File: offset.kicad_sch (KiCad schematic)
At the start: 52 parts

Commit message: More work in progres
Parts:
- removed C? (x3): 100n, symbol Device:C
- removed C? (x2): 1u, symbol Device:C
- removed R? (x3): 100k, symbol Device:R
- removed R? (x6): 158, symbol Device:R
- removed R? (x3): 309, symbol Device:R
- removed R?: 10k2, symbol Device:R
- removed R? (x2): 620, symbol Device:R
- removed R?: 80k6, symbol Device:R
- removed R?: 40k1, symbol Device:R
- removed R? (x2): 2k49, symbol Device:R
- removed R? (x2): 100, symbol Device:R
- removed R?: 20k, symbol Device:R
- removed R?: 1k24, symbol Device:R
- removed U? (x3): OPA2189D, Package_SO:SOIC-8_3.9x4.9mm_P1.27mm, symbol Parts:OPA2189D
- removed U? (x2): DG408, Package_SO:TSSOP-16_4.4x5mm_P0.65mm, symbol Analog_Switch:ADG1408YRUZ
- added C103, C?: 100n, symbol Device:C
- added D? (x2): 1N5819WS, Diode_SMD:D_SOD-323, symbol Diode:1N5819WS
- added R101, R102, R103, R109: 604, Resistor_SMD:R_0603_1608Metric, symbol Device:R
- added R105, R106, R107, R110, R111, R112: 100, Resistor_SMD:R_0603_1608Metric, symbol Device:R
- added R108: 48k1, Resistor_SMD:R_0603_1608Metric, symbol Device:R
- added R113: 1k29, Resistor_SMD:R_0603_1608Metric, symbol Device:R
- added R?: 1k, Resistor_SMD:R_0402_1005Metric, symbol Device:R
- added U?: TMUX1108PW, Package_SO:TSSOP-16_4.4x5mm_P0.65mm, symbol Analog_Switch:TMUX1108PW
- added U? (x3): OPA2197xD, Package_SO:SOIC-8_3.9x4.9mm_P1.27mm, symbol Amplifier_Operational:OPA2197xD
- C105, C106: renamed from C?; now not fitted
- R104: renamed from R?; value 1k24 -> 604; footprint (none) -> Resistor_SMD:R_0603_1608Metric
- R114, R115: renamed from R?; footprint (none) -> Resistor_SMD:R_0402_1005Metric
- R116, R117: renamed from R?; footprint (none) -> Resistor_SMD:R_0805_2012Metric
- gave numbers to parts that had none: 10
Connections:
- net OffsetMux is gone; now on net GNDPWR: U11.3 (+)
- net PGND is gone; now on net GNDPWR: C105.2, C106.1, C107.2, C108.1, C109.2, C110.1
- net +5VA: now also D?.1 (K), U?.13 (VDD), U?.2 (EN)
- net A0: now also U?.1 (A0)
- net A1: now also U?.16 (A1)
- net A2: now also U?.15 (A2)
- net OffsetOut: now also C?.1, U?.3 (+), U?.8 (D); no longer U11.1, U11.2 (-)
- net 1V66: now reaches R104.1
- net 1V66: now also R103.1, U?.10 (S7)
- net GNDPWR: now reaches U11.4 (V-)
- net GNDPWR: now also C103.2, D?.2 (A), U?.14 (GND), U?.3 (VSS)
- net +18V: now reaches U11.8 (V+)
- net +18V: now also C103.1
- net ScanOut: now reaches U18.1 (COM)
- net AGND renamed GND
- net GND: now also R107.2, R112.2, R113.1, U?.4 (S1)
- net OP1V25 renamed 0V55
- net 0V55: now also R105.1, U?.11 (S6)
- net OP5V renamed 5V
- net 5V: now also R101.1, R108.1, U?.9 (S8)
- new net: R101.2, R102.2
- new net: C?.2, D?.1 (K), D?.2 (A), R?.1
- new net: R105.2, R106.2
- new net: R102.1, R103.2
- new net: R?.2, U?.1, U?.2 (-)
- new net: R110.2, R111.2
- new net: U11.1, U11.2 (-)
- new net -2V5: R113.2
- new net 0V01: R111.1, R112.1, U?.5 (S2)
- new net 0V03: U?.6 (S3)
- new net 0V09: R108.2, R109.1, U?.7 (S4)
- new net 0V18: R106.1, R107.1, U?.12 (S5)
- new net OV03: R109.2, R110.1
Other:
- moved on the sheet: C104, C107, C108, C109, C110, R104, R115, R116, R117, U11A, U11C, U18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

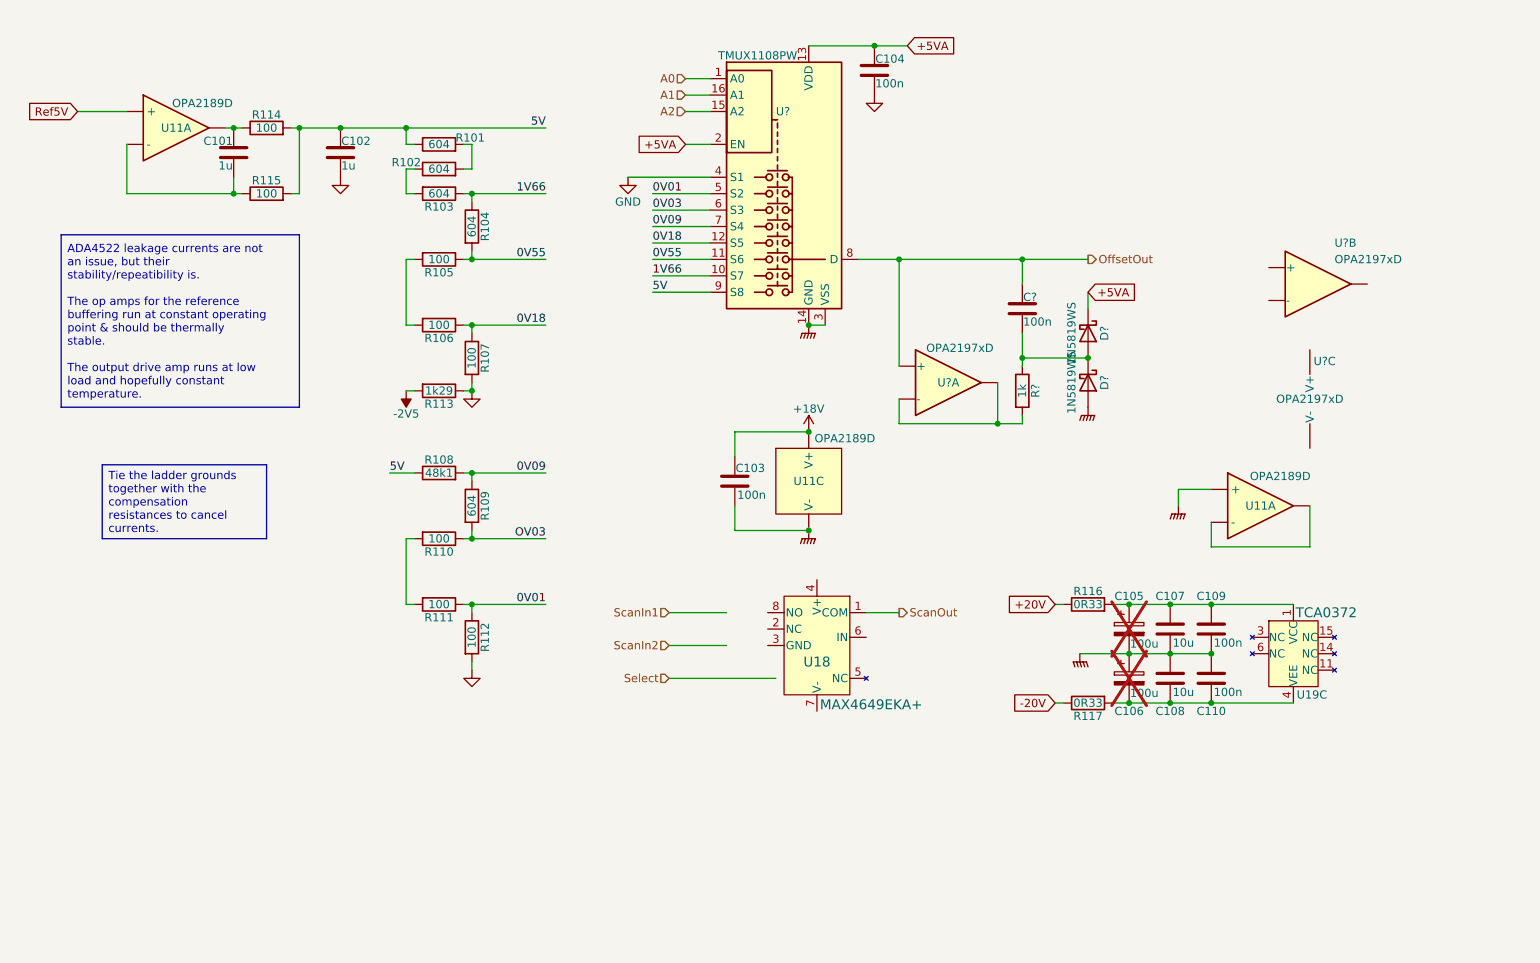
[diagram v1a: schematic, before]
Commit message: Analog side is more or less complete.
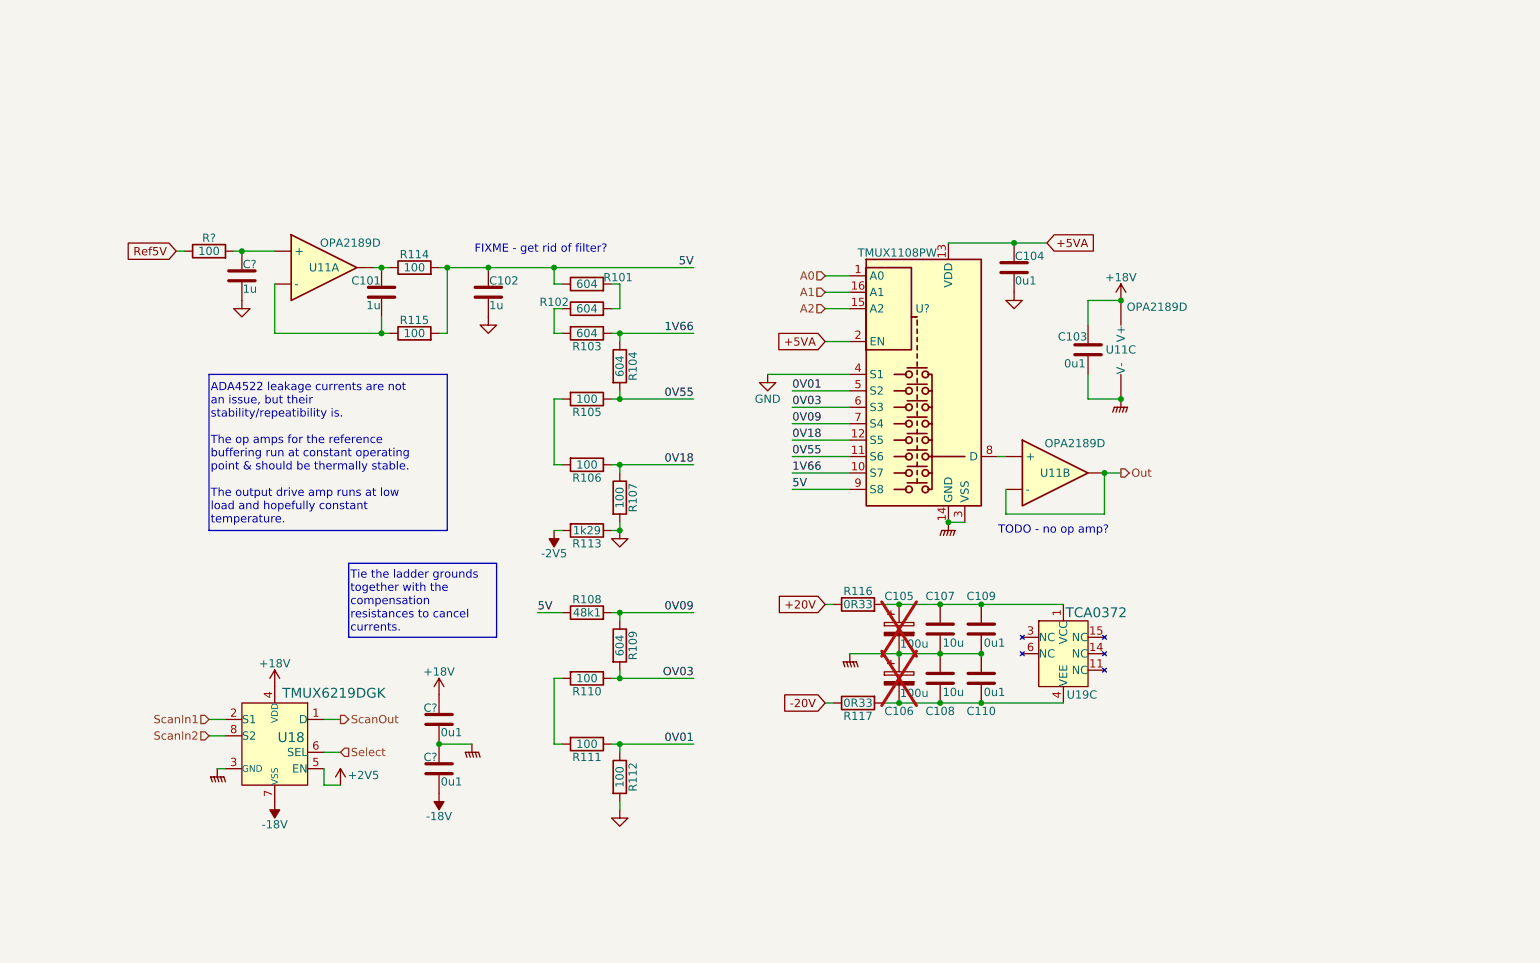
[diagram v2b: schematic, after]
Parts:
- removed C?: 100n, symbol Device:C
- removed D? (x2): 1N5819WS, Diode_SMD:D_SOD-323, symbol Diode:1N5819WS
- removed R?: 1k, Resistor_SMD:R_0402_1005Metric, symbol Device:R
- removed U? (x3): OPA2197xD, Package_SO:SOIC-8_3.9x4.9mm_P1.27mm, symbol Amplifier_Operational:OPA2197xD
- added C? (x2): 0u1, symbol Device:C
- added C?: 1u, symbol Device:C
- added R?: 100, Resistor_SMD:R_0402_1005Metric, symbol Device:R
- C103, C104, C109, C110: value 100n -> 0u1
- U18: value MAX4649EKA+ -> TMUX6219DGK; footprint 21-0078H_MXM -> SOIC8_DGK_TEX; symbol Parts:MAX4649EKA+ -> Parts:TMUX6219DGK
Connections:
- net +18V: now also U18.4 (VDD), C?.1
- net GND: now also C?.2
- net GNDPWR: now also U18.3 (GND), C?.1, C?.2; no longer U11.3 (+)
- net Ref5V: now also R?.1; no longer U11.3 (+)
- net ScanIn1: now also U18.2 (S1)
- net ScanIn2: now also U18.8 (S2)
- net Select: now also U18.6 (SEL)
- net +2V5: now reaches U18.5 (EN)
- net -18V: now reaches U18.7 (VSS)
- net -18V: now also C?.2
- net OffsetOut: no longer names the net of U?.8 (D)
- net OffsetOut: now also U11.5 (+)
- new net: C?.1, R?.2, U11.3 (+)
- new net Out: U11.6 (-), U11.7
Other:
- note added: "FIXME - get rid of filter?"
- note added: "TODO - no op amp?"
- moved on the sheet: C101, C102, C103, C104, C105, C106, C107, C108, C109, C110, R101, R102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

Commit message: Schematic complete, maybe
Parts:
- added L11, L12: 100, Inductor_SMD:L_0603_1608Metric, symbol Parts:L_Ferrite_Power
- added R119: 24k9, Resistor_SMD:R_0603_1608Metric, symbol Device:R
- added R120: 150k, Resistor_SMD:R_0603_1608Metric, symbol Device:R
- added R121: 1M5, Resistor_SMD:R_0603_1608Metric, symbol Device:R
- C101: renamed from C?; footprint (none) -> Capacitor_SMD:C_0402_1005Metric; LCSC (none) -> C52923
- C102: renamed from C101; footprint (none) -> Capacitor_SMD:C_0402_1005Metric; LCSC (none) -> C52923
- C103: renamed from C102; footprint (none) -> Capacitor_SMD:C_0402_1005Metric; LCSC (none) -> C52923
- C104: footprint (none) -> Capacitor_SMD:C_0402_1005Metric; LCSC (none) -> C307331
- C105: renamed from C103; footprint (none) -> Capacitor_SMD:C_0402_1005Metric; LCSC (none) -> C307331
- C106, C107: renamed from C?; footprint (none) -> Capacitor_SMD:C_0402_1005Metric; LCSC (none) -> C307331
- C108: renamed from C105; now left out of the parts list
- C109: renamed from C106; now left out of the parts list
- C110: renamed from C107; footprint (none) -> Capacitor_SMD:C_0805_2012Metric; LCSC (none) -> C440198
- C111: renamed from C108; footprint (none) -> Capacitor_SMD:C_0805_2012Metric; LCSC (none) -> C440198
- C112: renamed from C109; footprint (none) -> Capacitor_SMD:C_0402_1005Metric; LCSC (none) -> C307331
- C113: renamed from C110; footprint (none) -> Capacitor_SMD:C_0402_1005Metric; LCSC (none) -> C307331
- R101, R102, R103, R104, R105, R106, R107, R109, R110, R111, R112, U19: now left out of the parts list
- R108: value 48k1 -> 47k5; now left out of the parts list
- R118: renamed from R113; value 1k29 -> 1k37
- U11: LCSC (none) -> C881489; now left out of the parts list
- U12: renamed from U?; LCSC (none) -> C1021800; now left out of the parts list
- U18: LCSC (none) -> C2876423
- gave numbers to parts that had none: 1
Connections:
- net OV03 is gone; now on net 0V03: R109.2, R110.1
- net +20V: now also L11.1; no longer R116.1
- net -20V: now also L12.1; no longer R117.1
- net -2V5: now also R119.2, R120.1, R121.1
- net GND: now also R119.1, R120.2, R121.2
- net GNDPWR: now also U11.5 (+)
- net Out: now also U12.8 (D); no longer U11.6 (-), U11.7
- new net: L12.2, R117.1
- new net: L11.2, R116.1
- new net: U11.6 (-), U11.7
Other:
- note added: "FIXME - revisit filter?"
- note removed: "FIXME - get rid of filter?"
- note removed: "TODO - no op amp?"
- moved on the sheet: C105, C108, C109, C110, C111, C112, C113, R116, R117, U11B, U11C, U19C

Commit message: Part selection
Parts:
- R113, R114, R115: LCSC (none) -> C25076
- R116, R117, R118, R119: now left out of the parts list
- R120: LCSC (none) -> C22807
- R121: LCSC (none) -> C4172
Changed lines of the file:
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@@
 		(lib_id "Device:R")
 		(at 128.27 143.51 270)
+		(mirror x)
 		(unit 1)
 		(exclude_from_sim no)
-		(in_bom yes)
+		(in_bom no)
 		(on_board yes)
 		(dnp no)
 		(property "Reference" "R119"
-			(at 128.27 145.542 90)
+			(at 128.27 141.478 90)
 			(effects
 				(font
@@
 		)
 		(property "Footprint" "Resistor_SMD:R_0603_1608Metric"
-			(at 128.27 141.732 90)
+			(at 128.27 145.288 90)
 			(effects
 				(font
@@
 		(lib_id "Device:R")
 		(at 172.72 125.73 90)
-		(mirror x)
 		(unit 1)
 		(exclude_from_sim no)
-		(in_bom yes)
+		(in_bom no)
 		(on_board yes)
 		(dnp no)
 		(property "Reference" "R117"
-			(at 172.72 127.762 90)
+			(at 172.72 123.698 90)
 			(effects
 				(font
@@
 		)
 		(property "Footprint" "Resistor_SMD:R_0805_2012Metric"
-			(at 172.72 123.952 90)
+			(at 172.72 127.508 90)
 			(effects
 				(font
@@
 		(lib_id "Device:R")
 		(at 128.27 90.17 270)
+		(mirror x)
 		(unit 1)
 		(exclude_from_sim no)
@@
 		(dnp no)
 		(property "Reference" "R106"
-			(at 128.27 92.202 90)
+			(at 128.27 88.138 90)
 			(effects
 				(font
@@
 		)
 		(property "Footprint" "Resistor_SMD:R_0603_1608Metric"
-			(at 128.27 88.392 90)
+			(at 128.27 91.948 90)
 			(effects
 				(font
@@
 			)
 		)
+		(property "LCSC" "C25076"
+			(at 101.6 59.69 90)
+			(effects
+				(font
+					(size 1.27 1.27)
+				)
+				(hide yes)
+			)
+		)
 		(pin "1"
 		)
@@
 		(lib_id "Device:R")
 		(at 128.27 100.33 270)
+		(mirror x)
 		(unit 1)
 		(exclude_from_sim no)
-		(in_bom yes)
+		(in_bom no)
 		(on_board yes)
 		(dnp no)
 		(property "Reference" "R118"
-			(at 128.27 102.362 90)
+			(at 128.27 98.298 90)
 			(effects
 				(font
@@
 		)
 		(property "Footprint" "Resistor_SMD:R_0603_1608Metric"
-			(at 128.27 98.552 90)
+			(at 128.27 102.108 90)
 			(effects
 				(font
@@
 		(lib_id "Device:R")
 		(at 128.27 133.35 270)
+		(mirror x)
 		(unit 1)
 		(exclude_from_sim no)
@@
 		(dnp no)
 		(property "Reference" "R111"
-			(at 128.27 135.382 90)
+			(at 128.27 131.318 90)
 			(effects
 				(font
@@
 		)
 		(property "Footprint" "Resistor_SMD:R_0603_1608Metric"
-			(at 128.27 131.572 90)
+			(at 128.27 135.128 90)
 			(effects
 				(font
@@
 		(unit 1)
 		(exclude_from_sim no)
-		(in_bom yes)
+		(in_bom no)
 		(on_board yes)
 		(dnp no)
@@
 		(lib_id "Device:R")
 		(at 128.27 123.19 270)
+		(mirror x)
 		(unit 1)
 		(exclude_from_sim no)
@@
 		(dnp no)
 		(property "Reference" "R110"
-			(at 128.27 125.222 90)
+			(at 128.27 121.158 90)
 			(effects
 				(font
@@
 		)
 		(property "Footprint" "Resistor_SMD:R_0603_1608Metric"
-			(at 128.27 121.412 90)
+			(at 128.27 124.968 90)
 			(effects
 				(font
@@
 			)
 		)
+		(property "LCSC" "C22807"
+			(at 138.43 100.33 90)
+			(effects
+				(font
+					(size 1.27 1.27)
+				)
+				(hide yes)
+			)
+		)
 		(pin "2"
 		)
@@
 			)
 		)
+		(property "LCSC" "C4172"
+			(at 138.43 143.51 90)
+			(effects
+				(font
+					(size 1.27 1.27)
+				)
+				(hide yes)
+			)
+		)
 		(pin "2"
 		)
@@
 			)
 		)
+		(property "LCSC" "C25076"
+			(at 69.85 57.15 90)
+			(effects
+				(font
+					(size 1.27 1.27)
+				)
+				(hide yes)
+			)
+		)
 		(pin "1"
 		)
@@
 			(effects
 				(font
+					(size 1.27 1.27)
+				)
+				(hide yes)
+			)
+		)
+		(property "LCSC" "C25076"
+			(at 101.6 69.85 90)
+			(effects
+				(font

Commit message: ERC passes.
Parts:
- removed C102, C103: 1u, Capacitor_SMD:C_0402_1005Metric, symbol Device:C
- removed C108, C109: 100u, symbol Device:C_Polarized
- removed R114, R115: 100, Resistor_SMD:R_0402_1005Metric, symbol Device:R
- U11: value OPA2189D -> OPA2189DGK; footprint Package_SO:SOIC-8_3.9x4.9mm_P1.27mm -> Package_SO:MSOP-8_3x3mm_P0.65mm; symbol Parts:OPA2189D -> Parts:OPA2189DGK
- U18: footprint SOIC8_DGK_TEX -> Package_SO:VSSOP-8_3x3mm_P0.65mm
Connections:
- net 5V: now also U11.1, U11.2 (-)
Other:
- note removed: "FIXME - revisit filter?"
- moved on the sheet: C101, C105, C106, C107, C110, C111, C112, C113, L11, L12, R108, R109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
